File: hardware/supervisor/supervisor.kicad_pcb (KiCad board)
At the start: 2 copper layers, 149 parts, among them IC1 ULN2003A, IC2 LM2596-3.3, IC3 MAX11612, IC4 ACS723LLCTR-10AU-T, IC5 ACS723LLCTR-10AU-T, IC6 ACS723LLCTR-10AU-T, IC7 NLSX4373, IC8 NLSX4373, IC9 SIM900, K1 RELAY_SERIE_36, K2 RELAY_SERIE_36, P1 CONN_01X02, P2 RASPI-CONNECT, P3 POWER, P4 RELAY CONNECTOR, P5 CONN_01X02, P6 string0, P7 string1, P8 string2, P9 CONN_01X02, SW1 SW_PUSH, SW2 SW_PUSH, U1 SC16IS740IPW, U10 CD74HC4046, U11 CD74HC4046, U12 OPA376AIDCK, U13 CD74HC4046, U14 CD74HC4046, U2 SC16IS740IPW, U3 SC16IS740IPW, U4 RF_CONN, U5 SIM_HOLDER, U6 OPA376AIDCK, U7 CD74HC4046, U8 CD74HC4046, U9 OPA376AIDCK

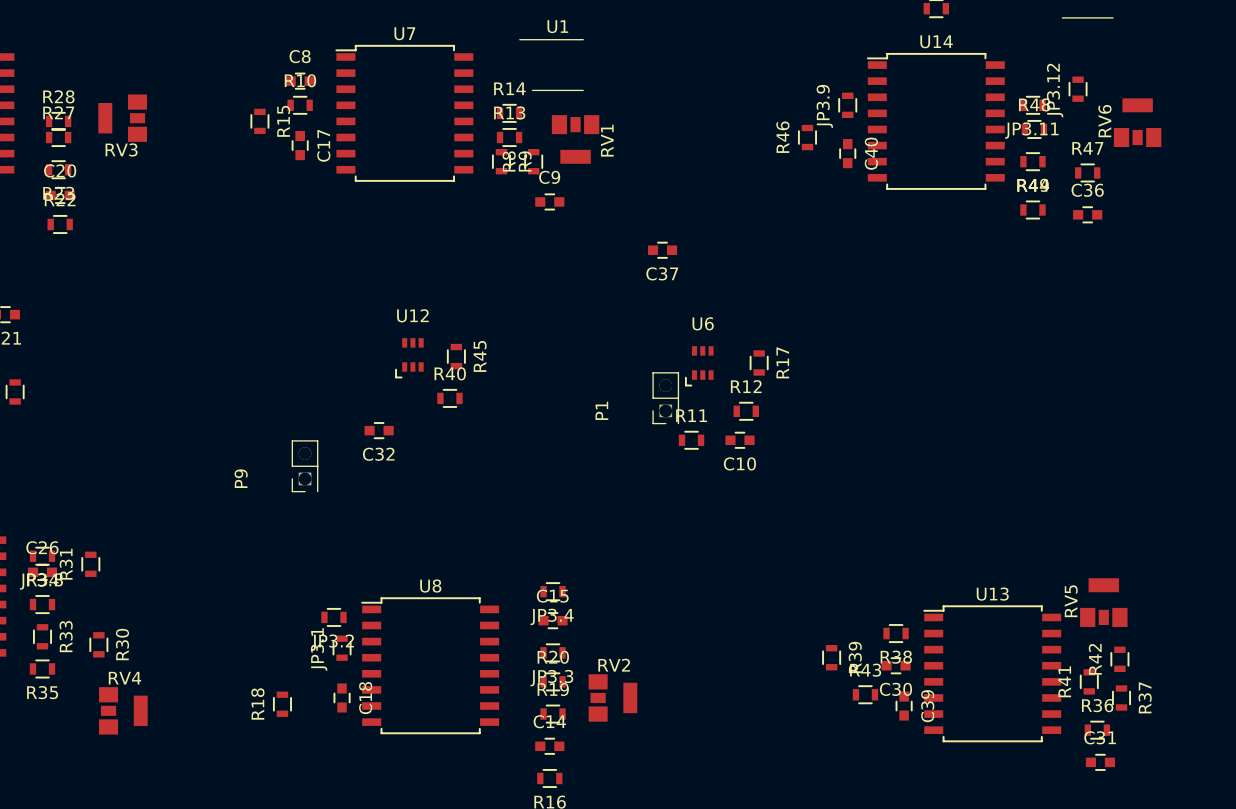
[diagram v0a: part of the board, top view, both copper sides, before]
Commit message: updated poti library from sensor libraries
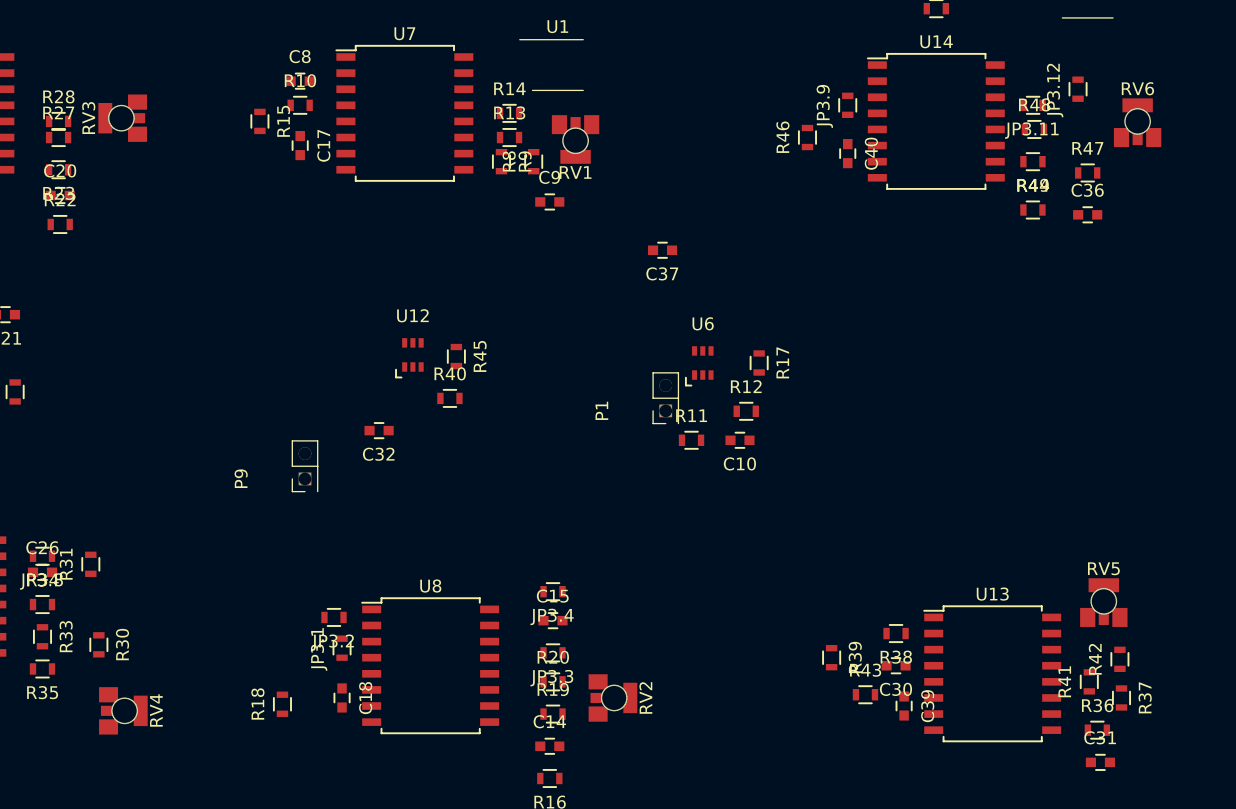
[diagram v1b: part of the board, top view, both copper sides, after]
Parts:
- RV1, RV2, RV3, RV4, RV5, RV6: footprint pro4:EVM-1USX30B14 -> pro4:EVM-1USX30B14_poti
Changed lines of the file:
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@@
-(kicad_pcb (version 4) (host pcbnew 4.0.2-stable)
+(kicad_pcb (version 4) (host pcbnew 4.0.2+dfsg1-stable)
   (general
     (links 383)
     (no_connects 262)
-    (area 0 -0.777 285.750001 233.934001)
+    (area 0 0 0 0)
     (thickness 1.6)
     (drawings 0)
@@
     )
   )
-  (module pro4:EVM-1USX30B14 (layer F.Cu)
-    (at 196.342 134.874 180)
-    (fp_text reference RV1 (at -2.54 0 270) (layer F.SilkS)
-      (effects (font (size 1 1) (thickness 0.15)))
-    )
-    (fp_text value POT (at 0 -2.54 180) (layer F.Fab) hide
-      (effects (font (size 1 1) (thickness 0.15)))
-    )
-    (pad 1 smd rect (at -1.27 1.27 180) (size 1.2 1.5) (layers F.Cu F.Paste F.Mask))
-    (pad 3 smd rect (at 1.27 1.27 180) (size 1.2 1.5) (layers F.Cu F.Paste F.Mask)
-      (net 95 "Net-(R14-Pad2)"))
-    (pad 4 smd rect (at 0 -1.27 180) (size 2.4 1.1) (layers F.Cu F.Paste F.Mask))
-    (pad 2 smd rect (at 0 1.27 180) (size 0.8 1.2) (layers F.Cu F.Paste F.Mask)
-      (net 2 GND))
-  )
-  (module pro4:EVM-1USX30B14 (layer F.Cu)
-    (at 199.39 178.816 270)
-    (fp_text reference RV2 (at -2.54 0 360) (layer F.SilkS)
-      (effects (font (size 1 1) (thickness 0.15)))
-    )
-    (fp_text value POT (at 0 -2.54 270) (layer F.Fab) hide
-      (effects (font (size 1 1) (thickness 0.15)))
-    )
-    (pad 1 smd rect (at -1.27 1.27 270) (size 1.2 1.5) (layers F.Cu F.Paste F.Mask)
-      (net 100 "Net-(R20-Pad2)"))
-    (pad 3 smd rect (at 1.27 1.27 270) (size 1.2 1.5) (layers F.Cu F.Paste F.Mask))
-    (pad 4 smd rect (at 0 -1.27 270) (size 2.4 1.1) (layers F.Cu F.Paste F.Mask))
-    (pad 2 smd rect (at 0 1.27 270) (size 0.8 1.2) (layers F.Cu F.Paste F.Mask)
-      (net 2 GND))
-  )
-  (module pro4:EVM-1USX30B14 (layer F.Cu)
-    (at 160.528 133.096 90)
-    (fp_text reference RV3 (at -2.54 0 180) (layer F.SilkS)
-      (effects (font (size 1 1) (thickness 0.15)))
-    )
-    (fp_text value POT (at 0 -2.54 90) (layer F.Fab) hide
-      (effects (font (size 1 1) (thickness 0.15)))
-    )
-    (pad 1 smd rect (at -1.27 1.27 90) (size 1.2 1.5) (layers F.Cu F.Paste F.Mask))
-    (pad 3 smd rect (at 1.27 1.27 90) (size 1.2 1.5) (layers F.Cu F.Paste F.Mask)
-      (net 104 "Net-(R28-Pad2)"))
-    (pad 4 smd rect (at 0 -1.27 90) (size 2.4 1.1) (layers F.Cu F.Paste F.Mask))
-    (pad 2 smd rect (at 0 1.27 90) (size 0.8 1.2) (layers F.Cu F.Paste F.Mask)
-      (net 2 GND))
-  )
-  (module pro4:EVM-1USX30B14 (layer F.Cu)
-    (at 160.782 179.832 270)
-    (fp_text reference RV4 (at -2.54 0 360) (layer F.SilkS)
-      (effects (font (size 1 1) (thickness 0.15)))
-    )
-    (fp_text value POT (at 0 -2.54 270) (layer F.Fab) hide
-      (effects (font (size 1 1) (thickness 0.15)))
-    )
-    (pad 1 smd rect (at -1.27 1.27 270) (size 1.2 1.5) (layers F.Cu F.Paste F.Mask)
-      (net 109 "Net-(R34-Pad2)"))
-    (pad 3 smd rect (at 1.27 1.27 270) (size 1.2 1.5) (layers F.Cu F.Paste F.Mask))
-    (pad 4 smd rect (at 0 -1.27 270) (size 2.4 1.1) (layers F.Cu F.Paste F.Mask))
-    (pad 2 smd rect (at 0 1.27 270) (size 0.8 1.2) (layers F.Cu F.Paste F.Mask)
-      (net 2 GND))
-  )
-  (module pro4:EVM-1USX30B14 (layer F.Cu)
-    (at 237.998 171.196)
-    (fp_text reference RV5 (at -2.54 0 90) (layer F.SilkS)
-      (effects (font (size 1 1) (thickness 0.15)))
-    )
-    (fp_text value POT (at 0 -2.54) (layer F.Fab) hide
-      (effects (font (size 1 1) (thickness 0.15)))
-    )
-    (pad 1 smd rect (at -1.27 1.27) (size 1.2 1.5) (layers F.Cu F.Paste F.Mask))
-    (pad 3 smd rect (at 1.27 1.27) (size 1.2 1.5) (layers F.Cu F.Paste F.Mask)
-      (net 113 "Net-(R42-Pad2)"))
-    (pad 4 smd rect (at 0 -1.27) (size 2.4 1.1) (layers F.Cu F.Paste F.Mask))
-    (pad 2 smd rect (at 0 1.27) (size 0.8 1.2) (layers F.Cu F.Paste F.Mask)
-      (net 2 GND))
-  )
-  (module pro4:EVM-1USX30B14 (layer F.Cu)
-    (at 240.665 133.35)
-    (fp_text reference RV6 (at -2.54 0 90) (layer F.SilkS)
-      (effects (font (size 1 1) (thickness 0.15)))
-    )
-    (fp_text value POT (at 0 -2.54) (layer F.Fab) hide
-      (effects (font (size 1 1) (thickness 0.15)))
-    )
-    (pad 1 smd rect (at -1.27 1.27) (size 1.2 1.5) (layers F.Cu F.Paste F.Mask)
-      (net 118 "Net-(R48-Pad2)"))
-    (pad 3 smd rect (at 1.27 1.27) (size 1.2 1.5) (layers F.Cu F.Paste F.Mask))
-    (pad 4 smd rect (at 0 -1.27) (size 2.4 1.1) (layers F.Cu F.Paste F.Mask))
-    (pad 2 smd rect (at 0 1.27) (size 0.8 1.2) (layers F.Cu F.Paste F.Mask)
-      (net 2 GND))
-  )
   (module TO_SOT_Packages_SMD:SC-70-6 (layer F.Cu)
     (at 206.375 152.4)
@@
     )
   )
+  (module pro4:EVM-1USX30B14_poti placed (layer F.Cu)
+    (at 196.342 134.874 180)
+    (fp_text reference RV1 (at 0 -2.54 360) (layer F.SilkS)
+      (effects (font (size 1 1) (thickness 0.15)))
+    )
+    (fp_text value POT (at 0 -2.54 180) (layer F.Fab) hide
+      (effects (font (size 1 1) (thickness 0.15)))
+    )
+    (pad 1 smd rect (at -1.27 1.27 180) (size 1.2 1.5) (layers F.Cu F.Paste F.Mask))
+    (pad 3 smd rect (at 1.27 1.27 180) (size 1.2 1.5) (layers F.Cu F.Paste F.Mask)
+      (net 95 "Net-(R14-Pad2)"))
+    (pad 4 smd rect (at 0 -1.27 180) (size 2.4 1.1) (layers F.Cu F.Paste F.Mask))
+    (pad 2 smd rect (at 0 1.27 180) (size 0.8 1.2) (layers F.Cu F.Paste F.Mask)
+      (net 2 GND))
+    (pad "" np_thru_hole circle (at 0 0 180) (size 2 2) (drill 2) (layers *.Cu *.Mask F.SilkS))
+  )
+  (module pro4:EVM-1USX30B14_poti placed (layer F.Cu)
+    (at 199.39 178.816 270)
+    (fp_text reference RV2 (at 0 -2.54 450) (layer F.SilkS)
+      (effects (font (size 1 1) (thickness 0.15)))
+    )
+    (fp_text value POT (at 0 -2.54 270) (layer F.Fab) hide
+      (effects (font (size 1 1) (thickness 0.15)))
+    )
+    (pad 1 smd rect (at -1.27 1.27 270) (size 1.2 1.5) (layers F.Cu F.Paste F.Mask)
+      (net 100 "Net-(R20-Pad2)"))
+    (pad 3 smd rect (at 1.27 1.27 270) (size 1.2 1.5) (layers F.Cu F.Paste F.Mask))
+    (pad 4 smd rect (at 0 -1.27 270) (size 2.4 1.1) (layers F.Cu F.Paste F.Mask))
+    (pad 2 smd rect (at 0 1.27 270) (size 0.8 1.2) (layers F.Cu F.Paste F.Mask)
+      (net 2 GND))
+    (pad "" np_thru_hole circle (at 0 0 270) (size 2 2) (drill 2) (layers *.Cu *.Mask F.SilkS))
+  )
+  (module pro4:EVM-1USX30B14_poti placed (layer F.Cu)
+    (at 160.528 133.096 90)
+    (fp_text reference RV3 (at 0 -2.54 270) (layer F.SilkS)
+      (effects (font (size 1 1) (thickness 0.15)))
+    )
+    (fp_text value POT (at 0 -2.54 90) (layer F.Fab) hide
+      (effects (font (size 1 1) (thickness 0.15)))
+    )
+    (pad 1 smd rect (at -1.27 1.27 90) (size 1.2 1.5) (layers F.Cu F.Paste F.Mask))
+    (pad 3 smd rect (at 1.27 1.27 90) (size 1.2 1.5) (layers F.Cu F.Paste F.Mask)
+      (net 104 "Net-(R28-Pad2)"))
+    (pad 4 smd rect (at 0 -1.27 90) (size 2.4 1.1) (layers F.Cu F.Paste F.Mask))
+    (pad 2 smd rect (at 0 1.27 90) (size 0.8 1.2) (layers F.Cu F.Paste F.Mask)
+      (net 2 GND))
+    (pad "" np_thru_hole circle (at 0 0 90) (size 2 2) (drill 2) (layers *.Cu *.Mask F.SilkS))
+  )
+  (module pro4:EVM-1USX30B14_poti placed (layer F.Cu)
+    (at 160.782 179.832 270)
+    (fp_text reference RV4 (at 0 -2.54 450) (layer F.SilkS)
+      (effects (font (size 1 1) (thickness 0.15)))
+    )
+    (fp_text value POT (at 0 -2.54 270) (layer F.Fab) hide
+      (effects (font (size 1 1) (thickness 0.15)))
+    )
+    (pad 1 smd rect (at -1.27 1.27 270) (size 1.2 1.5) (layers F.Cu F.Paste F.Mask)
+      (net 109 "Net-(R34-Pad2)"))
+    (pad 3 smd rect (at 1.27 1.27 270) (size 1.2 1.5) (layers F.Cu F.Paste F.Mask))
+    (pad 4 smd rect (at 0 -1.27 270) (size 2.4 1.1) (layers F.Cu F.Paste F.Mask))
+    (pad 2 smd rect (at 0 1.27 270) (size 0.8 1.2) (layers F.Cu F.Paste F.Mask)
+      (net 2 GND))
+    (pad "" np_thru_hole circle (at 0 0 270) (size 2 2) (drill 2) (layers *.Cu *.Mask F.SilkS))
+  )
+  (module pro4:EVM-1USX30B14_poti placed (layer F.Cu)
+    (at 237.998 171.196)
+    (fp_text reference RV5 (at 0 -2.54 180) (layer F.SilkS)
+      (effects (font (size 1 1) (thickness 0.15)))
+    )
+    (fp_text value POT (at 0 -2.54) (layer F.Fab) hide
+      (effects (font (size 1 1) (thickness 0.15)))
+    )
+    (pad 1 smd rect (at -1.27 1.27) (size 1.2 1.5) (layers F.Cu F.Paste F.Mask))
+    (pad 3 smd rect (at 1.27 1.27) (size 1.2 1.5) (layers F.Cu F.Paste F.Mask)
+      (net 113 "Net-(R42-Pad2)"))
+    (pad 4 smd rect (at 0 -1.27) (size 2.4 1.1) (layers F.Cu F.Paste F.Mask))
+    (pad 2 smd rect (at 0 1.27) (size 0.8 1.2) (layers F.Cu F.Paste F.Mask)
+      (net 2 GND))
+    (pad "" np_thru_hole circle (at 0 0) (size 2 2) (drill 2) (layers *.Cu *.Mask F.SilkS))
+  )
+  (module pro4:EVM-1USX30B14_poti placed (layer F.Cu)
+    (at 240.665 133.35)
+    (fp_text reference RV6 (at 0 -2.54 180) (layer F.SilkS)
+      (effects (font (size 1 1) (thickness 0.15)))
+    )
+    (fp_text value POT (at 0 -2.54) (layer F.Fab) hide
+      (effects (font (size 1 1) (thickness 0.15)))
+    )
+    (pad 1 smd rect (at -1.27 1.27) (size 1.2 1.5) (layers F.Cu F.Paste F.Mask)
+      (net 118 "Net-(R48-Pad2)"))
+    (pad 3 smd rect (at 1.27 1.27) (size 1.2 1.5) (layers F.Cu F.Paste F.Mask))
+    (pad 4 smd rect (at 0 -1.27) (size 2.4 1.1) (layers F.Cu F.Paste F.Mask))
+    (pad 2 smd rect (at 0 1.27) (size 0.8 1.2) (layers F.Cu F.Paste F.Mask)
+      (net 2 GND))
+    (pad "" np_thru_hole circle (at 0 0) (size 2 2) (drill 2) (layers *.Cu *.Mask F.SilkS))
+  )
   (zone (net 2) (net_name GND) (layer F.Cu) (hatch edge 0.508)

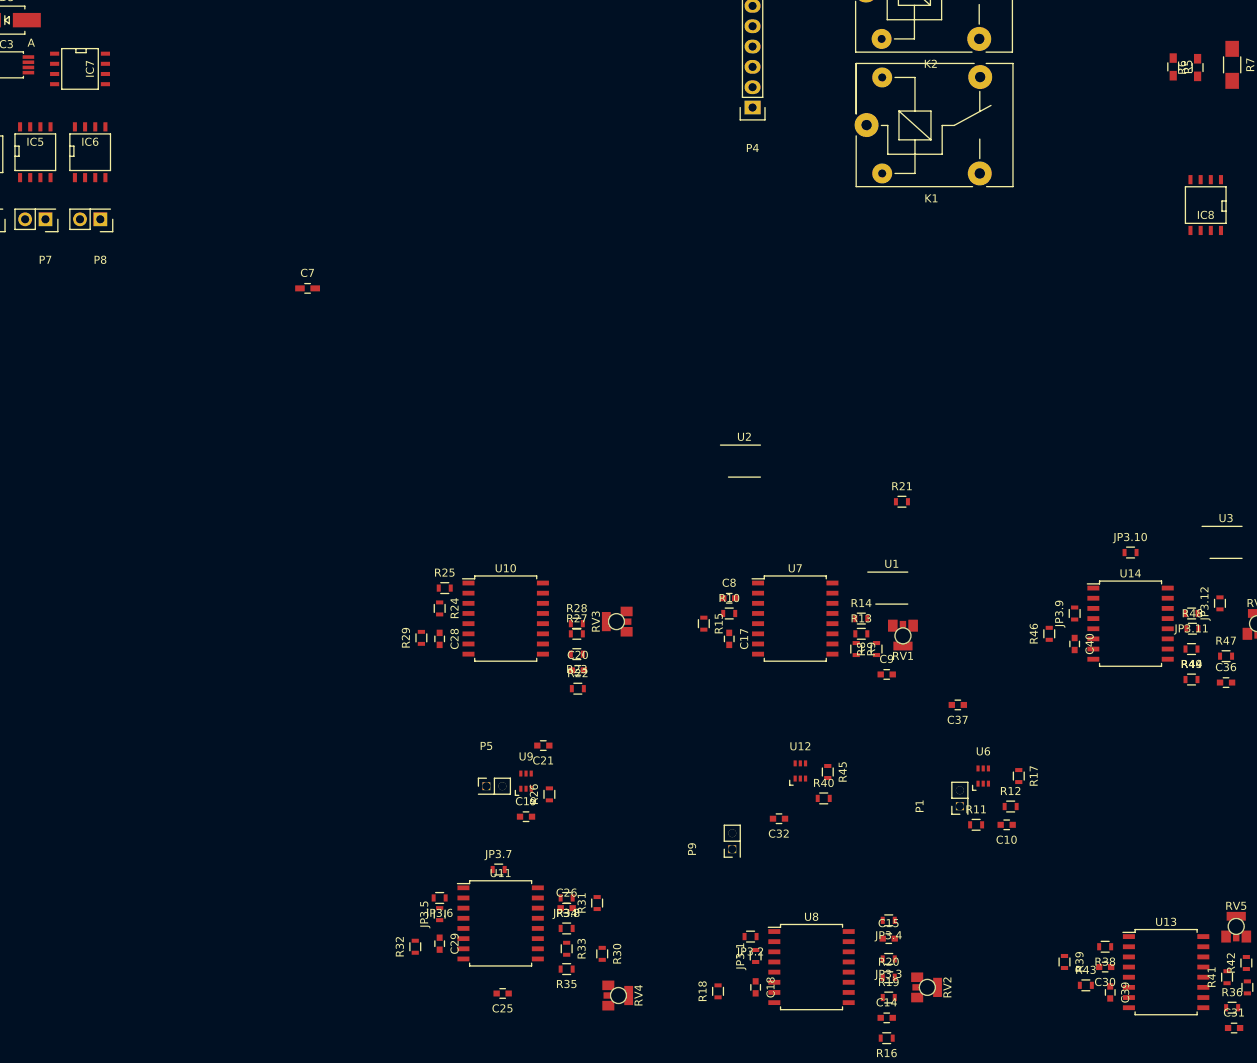
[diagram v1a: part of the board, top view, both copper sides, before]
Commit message: change PLL ic to thinner footprint
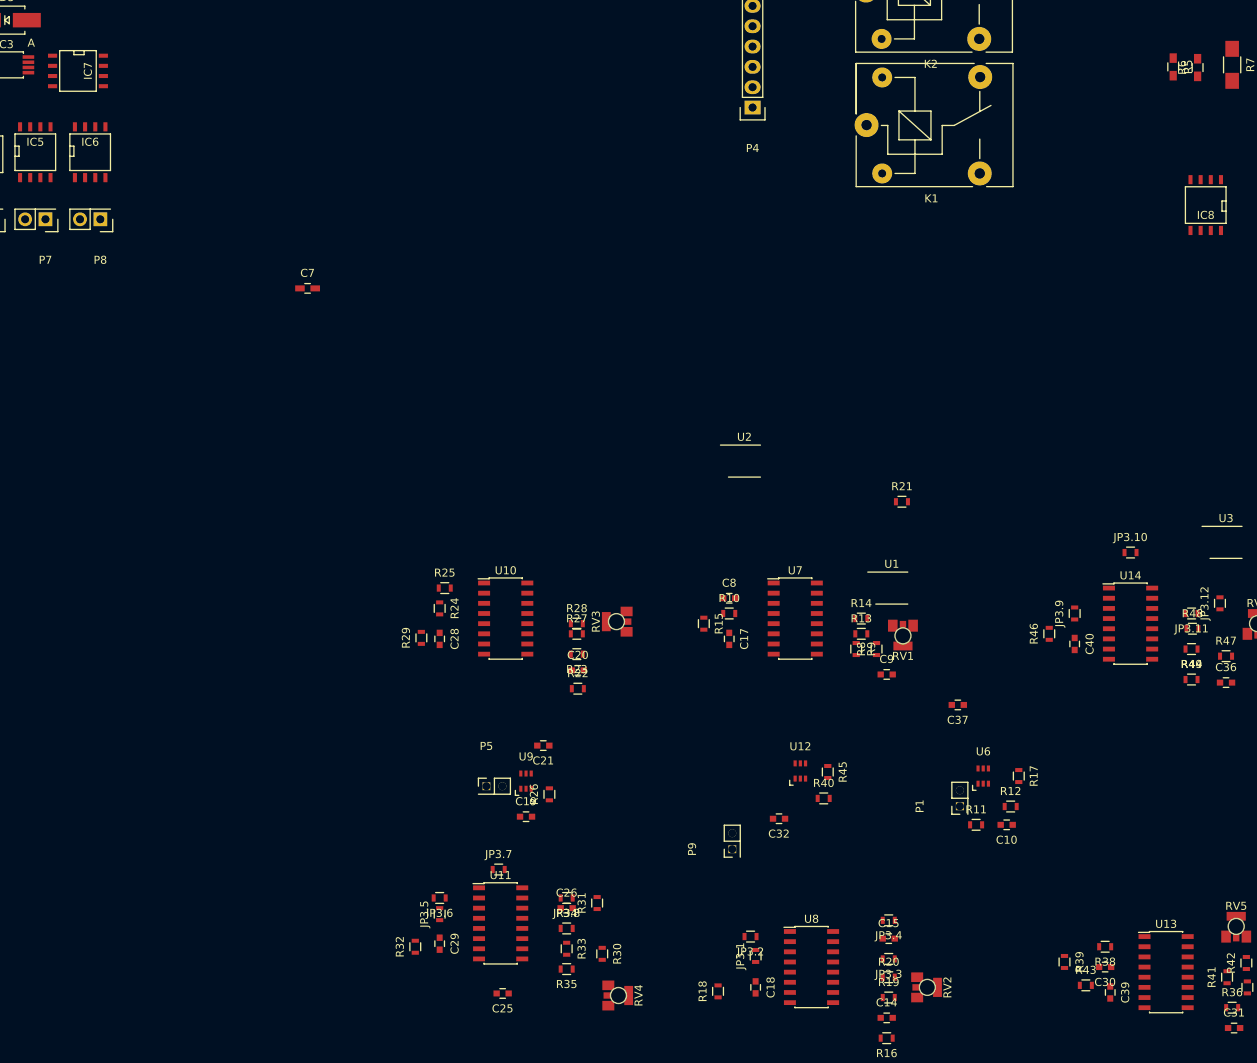
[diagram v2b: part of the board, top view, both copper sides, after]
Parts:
- U10, U11, U13, U14, U7, U8: footprint Housings_SOIC:SOIC-16_7.5x10.3mm_Pitch1.27mm -> Housings_SOIC:SOIC-16_3.9x9.9mm_Pitch1.27mm
- moved IC7 0.36 mm to (93.2, 64.3)
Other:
- net class Default: clearance 0.2 -> 0.25; trace_width 0.25 -> 0.2; via_dia 0.6 -> 1
- net class pro4_default removed
- net class pro4_hv removed
- rule trace_clearance: 0.2 -> 0.25
- rule via_min_drill: 0.3 -> 0.4
- rule via_min_size: 0.4 -> 1
